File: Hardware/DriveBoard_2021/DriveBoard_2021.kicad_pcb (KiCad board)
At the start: 2 copper layers, 124.5 x 101.6 mm, 89 parts, among them SW1 SW_Push, SW2 SW_Push, SW3 SW_Push, SW4 SW_Push, SW5 SW_Push, SW6 SW_Push, SW7 SW_Push, U1 LM2576S-3.3, U2 LM2576HVS-5, U3 TM4C129E_Launchpad, U4 MCP2551-I-SN

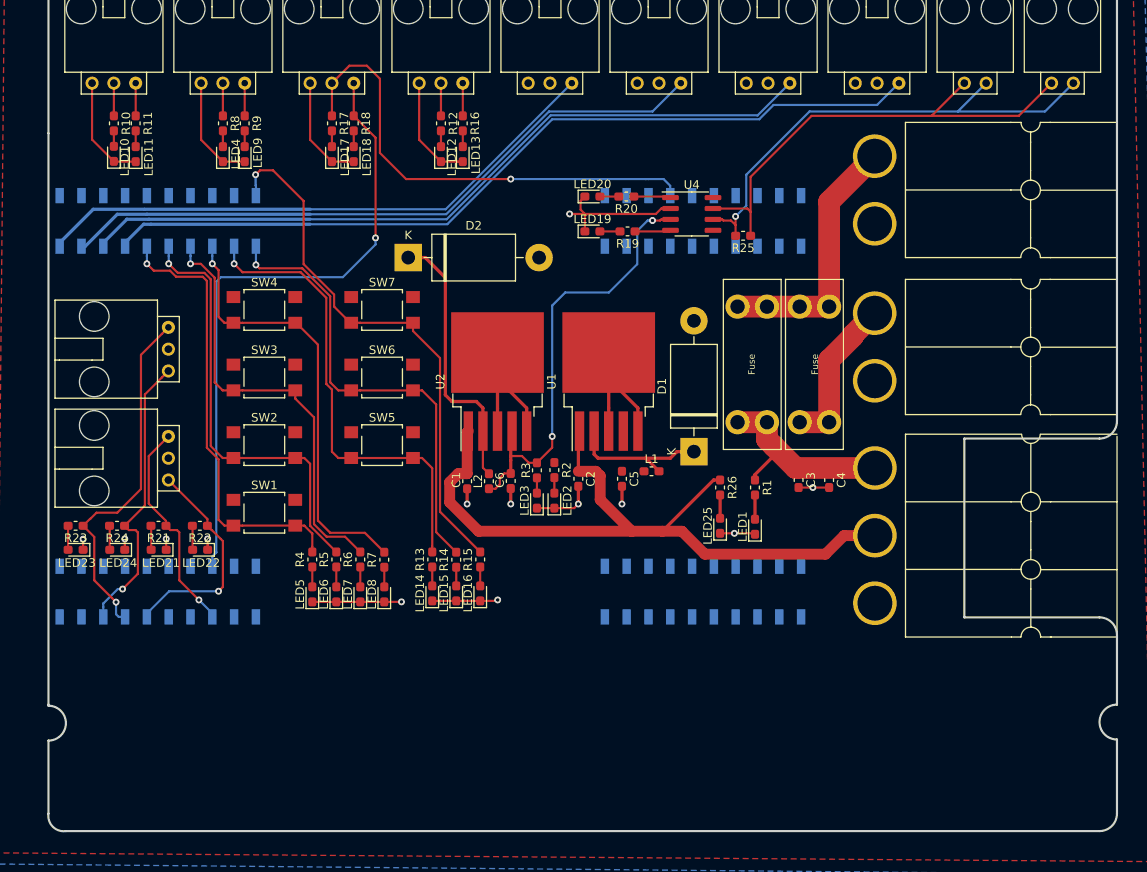
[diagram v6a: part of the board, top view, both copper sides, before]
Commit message: All Components and Traces Placed. Silkscreen Updated.
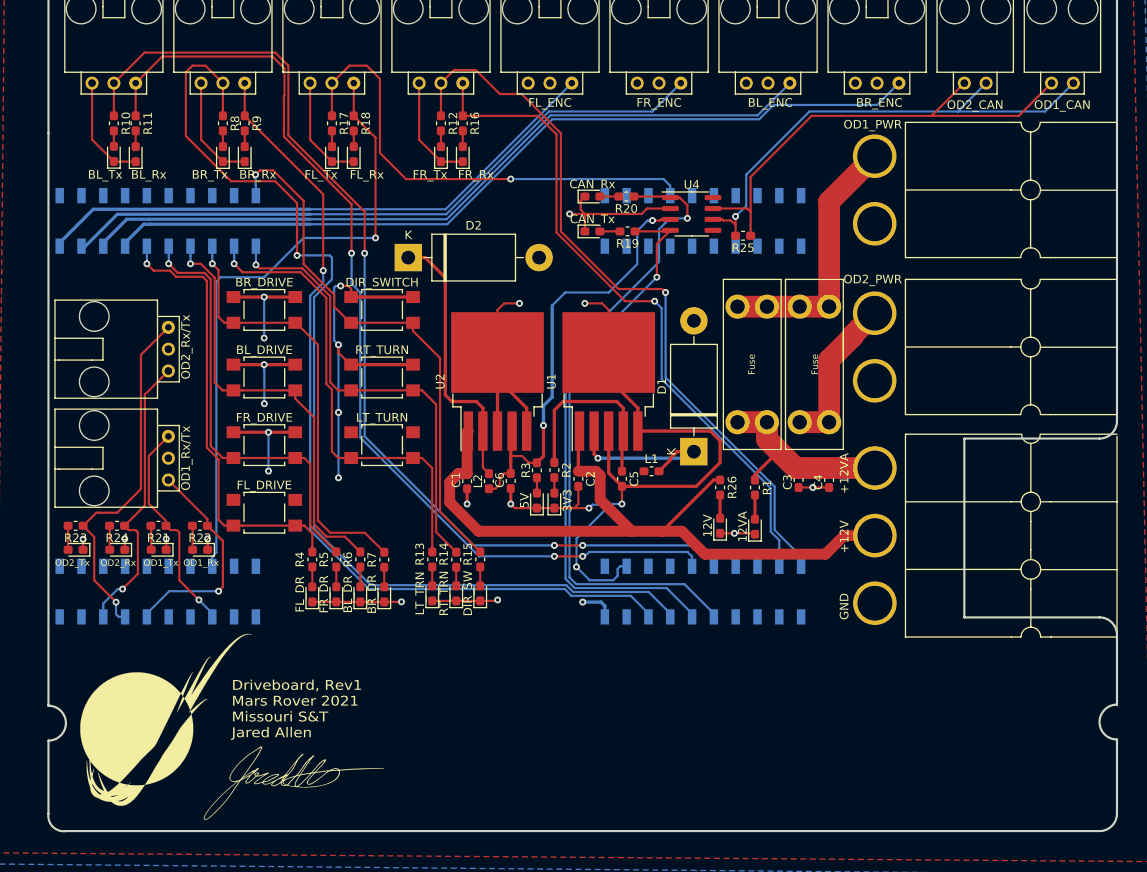
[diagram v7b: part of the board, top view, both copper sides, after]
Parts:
- added G***: LOGO, MRDT_Silkscreens:0_MRDT_Logo_20mm, F.Cu at (83.6, 139.7)
- added G***: LOGO, MRDT_Silkscreens:z_sig_Jared_Allen, F.Cu at (98.6, 147.1)
- renumbered LED25 to 12V, LED1 to 12VA, LED2 to 3V3, LED3 to 5V, LED7 to BL_DR, SW3 to BL_DRIVE, LED11 to BL_Rx, LED10 to BL_Tx, LED8 to BR_DR, SW4 to BR_DRIVE, LED9 to BR_Rx, LED4 to BR_Tx, LED20 to CAN_Rx, LED19 to CAN_Tx, LED16 to DIR_SW, SW7 to DIR_SWITCH, LED5 to FL_DR, SW1 to FL_DRIVE, LED18 to FL_Rx, LED17 to FL_Tx, LED6 to FR_DR, SW2 to FR_DRIVE, LED13 to FR_Rx, LED12 to FR_Tx, LED14 to LT_TRN, SW5 to LT_TURN, LED22 to OD1_Rx, LED21 to OD1_Tx, LED24 to OD2_Rx, LED23 to OD2_Tx, LED15 to RT_TRN, SW6 to RT_TURN
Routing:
- net BR_Tx: track 3.81 -> 121.6 mm, vias 0 -> 1
- net BL_Tx: track 3.81 -> 120.3 mm, vias 0 -> 3
- net BL_Rx: track 3.81 -> 115.7 mm, vias 0 -> 3
- net +3V3: track 0.22 -> 104.7 mm, vias 0 -> 11
- net BR_Rx: track 3.81 -> 100.3 mm, vias 0 -> 1
- net FR_Tx: track 3.81 -> 86.5 mm, vias 0 -> 1
- net FR_Rx: track 3.81 -> 78.7 mm, vias 0 -> 1
- net CAN_Rx: track 4.32 -> 74.0 mm, vias 0 -> 1
- net GND: track 150.5 -> 215.1 mm, vias 13 -> 16
- net CAN_Tx: track 4.18 -> 68.4 mm, vias 0 -> 1
- net Net-(D1-Pad1): track 17.0 -> 20.0 mm, vias 0 -> 1
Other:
- board text added: "+12V"
- board text added: "+12VA"
- board text added: "BL_ENC"
- board text added: "BR_ENC"
- board text added: "Driveboard, Rev1 Mars Rover 2021 Missouri S&T Jared Allen"
- board text added: "FL_ENC"
- board text added: "FR_ENC"
- board text added: "GND"
- board text added: "OD1_CAN"
- board text added: "OD1_PWR"
- board text added: "OD1_Rx/Tx"
- board text added: "OD2_CAN"
- board text added: "OD2_PWR"
- board text added: "OD2_Rx/Tx"

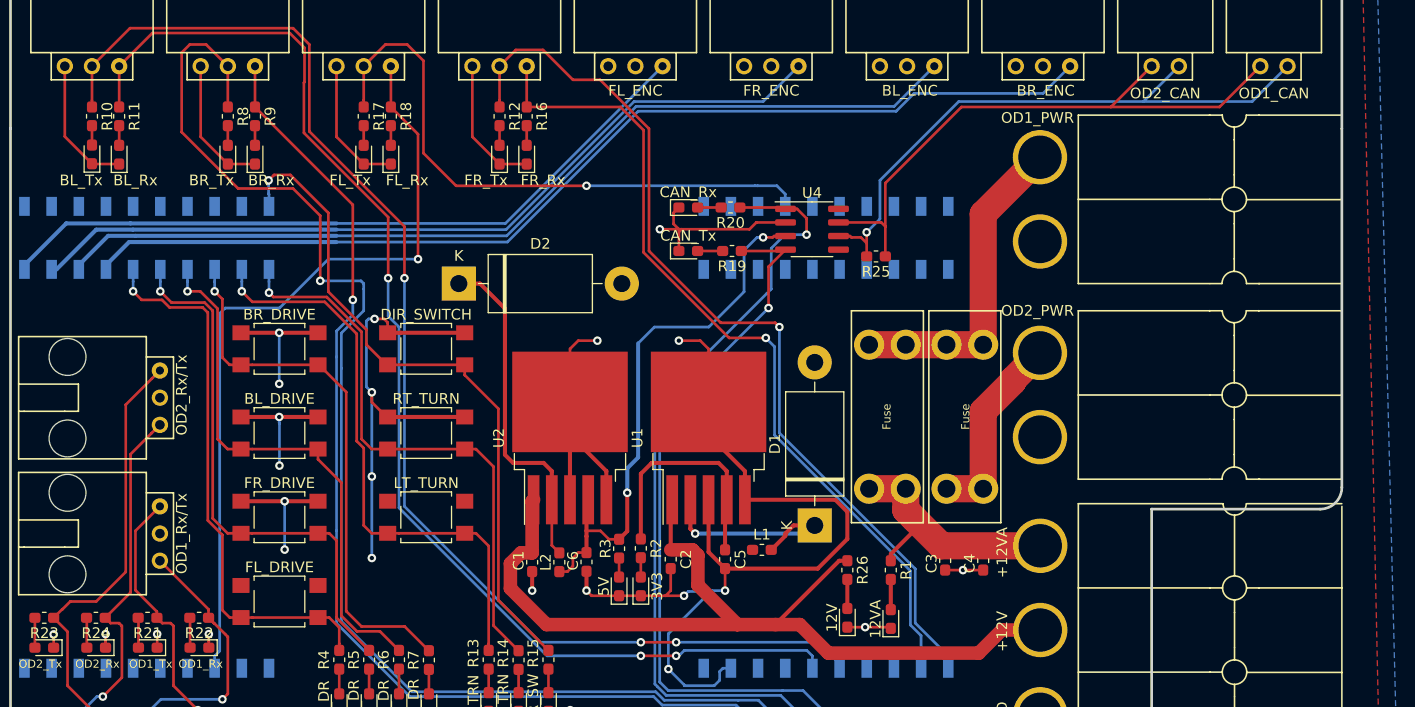
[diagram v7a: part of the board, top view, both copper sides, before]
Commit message: Changed Actuation trace width. Added gerbs and BOM to documentation. Added TIVA connections and board connectors text files.
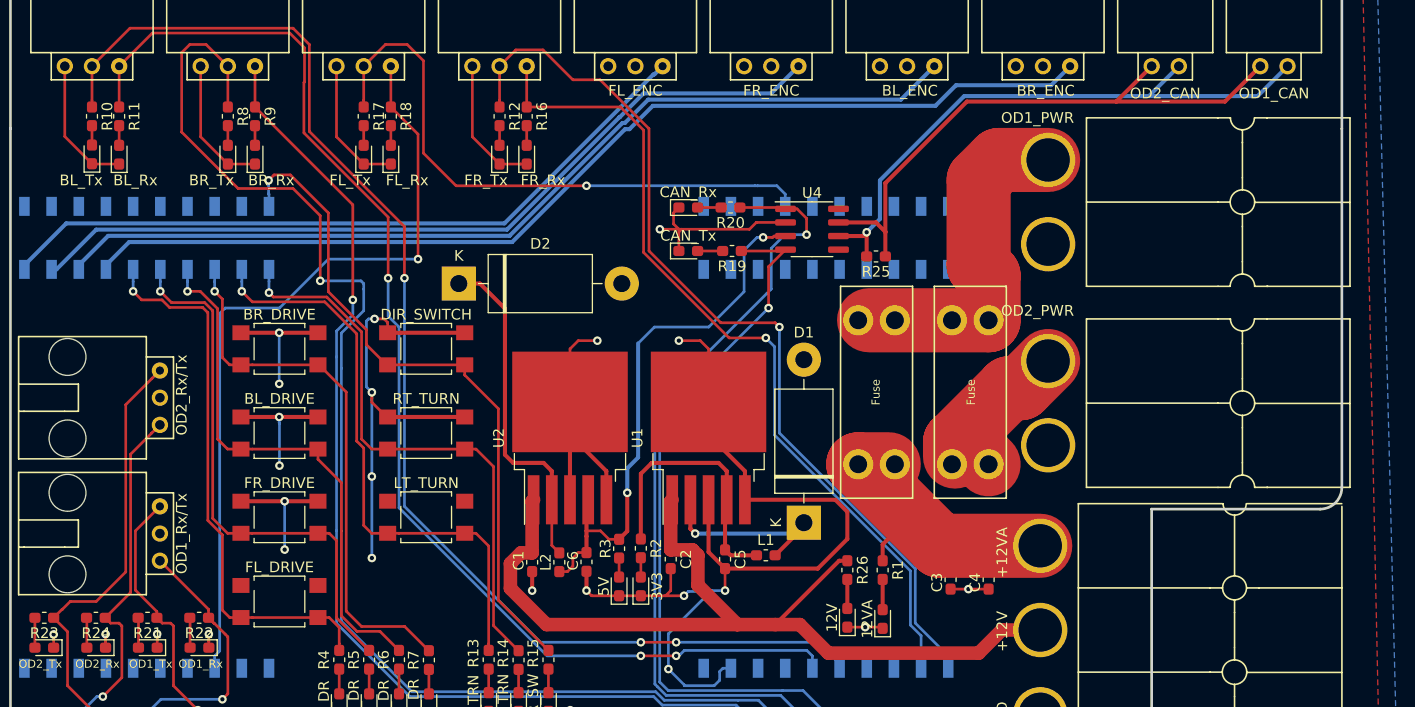
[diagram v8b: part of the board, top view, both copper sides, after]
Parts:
- moved F1 2.50 mm to (154.2, 105.9)
- moved F2 2.34 mm to (156.2, 86.1)
- moved C3 1.85 mm to (157.7, 113.5)
- moved C4 1.85 mm to (161.3, 113.5)
- moved Conn3 1.08 mm to (170.4, 89.2)
- moved D1 1.05 mm to (144.0, 108.2)
- moved Conn2 0.80 mm to (170.4, 70.4)
- moved 12VA 0.76 mm to (151.4, 117.2)
- moved R1 0.76 mm to (151.4, 112.6)
- moved L1 0.63 mm to (140.5, 111.3)
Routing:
- net +12VA: track 24.2 -> 29.0 mm
- net +3V3: track 104.7 -> 107.8 mm
- net Net-(Conn2-Pad2): track 30.4 -> 31.9 mm
- net Net-(Conn3-Pad2): track 18.3 -> 17.2 mm
- net Net-(D1-Pad1): track 20.0 -> 21.0 mm
- net CANL: track 57.7 -> 56.9 mm
- net GND: track 215.1 -> 214.6 mm
- net CANH: track 56.4 -> 55.9 mm
